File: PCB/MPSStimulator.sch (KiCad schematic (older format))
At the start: 38 parts

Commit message: WIP.
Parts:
- R? (x17): footprint Upper Center K -> (none); symbol Device:R_US -> Device:R; Notes O Bk Br Gd = 300Ω ±5% -> (none)
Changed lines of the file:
@@
 	4800 6250 4700 6250
 $Comp
-L Device:R_US R?
+L Device:R R?
 U 1 1 624C0ACD
 P 4700 6750
 F 0 "R?" H 4500 6800 50  0000 L CNN
 F 1 "180k" H 4450 6700 50  0000 L CNN
-F 2 "Upper Center K" V 4740 6740 50  0001 C CNN
+F 2 "" V 4740 6740 50  0001 C CNN
 F 3 "~" H 4700 6750 50  0001 C CNN
-F 4 "O Bk Br Gd = 300Ω ±5%" H 4700 6750 50  0001 C CNN "Notes"
+F 4 "" H 4700 6750 50  0001 C CNN "Notes"
 	1    4700 6750
 	1    0    0    1
@@
 Connection ~ 5100 7100
 $Comp
-L Device:R_US R?
+L Device:R R?
 U 1 1 625125B1
 P 5400 6550
 F 0 "R?" V 5500 6600 50  0000 L CNN
 F 1 "300" V 5500 6400 50  0000 L CNN
-F 2 "Upper Center K" V 5440 6540 50  0001 C CNN
+F 2 "" V 5440 6540 50  0001 C CNN
 F 3 "~" H 5400 6550 50  0001 C CNN
-F 4 "O Bk Br Gd = 300Ω ±5%" H 5400 6550 50  0001 C CNN "Notes"
+F 4 "" H 5400 6550 50  0001 C CNN "Notes"
 	1    5400 6550
 	0    1    1    0
@@
 	5800 6550 5550 6550
 $Comp
-L Device:R_US R?
+L Device:R R?
 U 1 1 6254B02E
 P 5400 5800
 F 0 "R?" V 5500 5850 50  0000 L CNN
 F 1 "2k4" V 5500 5700 50  0000 L CNN
-F 2 "Upper Center K" V 5440 5790 50  0001 C CNN
+F 2 "" V 5440 5790 50  0001 C CNN
 F 3 "~" H 5400 5800 50  0001 C CNN
-F 4 "O Bk Br Gd = 300Ω ±5%" H 5400 5800 50  0001 C CNN "Notes"
+F 4 "" H 5400 5800 50  0001 C CNN "Notes"
 	1    5400 5800
 	0    1    1    0
@@
 	5100 7100 6300 7100
 $Comp
-L Device:R_US R?
+L Device:R R?
 U 1 1 625BF40D
 P 5100 5250
 F 0 "R?" H 4900 5300 50  0000 L CNN
 F 1 "2k" H 4900 5200 50  0000 L CNN
-F 2 "Upper Center K" V 5140 5240 50  0001 C CNN
+F 2 "" V 5140 5240 50  0001 C CNN
 F 3 "~" H 5100 5250 50  0001 C CNN
-F 4 "O Bk Br Gd = 300Ω ±5%" H 5100 5250 50  0001 C CNN "Notes"
+F 4 "" H 5100 5250 50  0001 C CNN "Notes"
 	1    5100 5250
 	1    0    0    1
 $EndComp
 $Comp
-L Device:R_US R?
+L Device:R R?
 U 1 1 625C0721
 P 6300 5250
 F 0 "R?" H 6100 5300 50  0000 L CNN
 F 1 "1k" H 6100 5200 50  0000 L CNN
-F 2 "Upper Center K" V 6340 5240 50  0001 C CNN
+F 2 "" V 6340 5240 50  0001 C CNN
 F 3 "~" H 6300 5250 50  0001 C CNN
-F 4 "O Bk Br Gd = 300Ω ±5%" H 6300 5250 50  0001 C CNN "Notes"
+F 4 "" H 6300 5250 50  0001 C CNN "Notes"
 	1    6300 5250
 	1    0    0    1
@@
 Connection ~ 6300 7100
 $Comp
-L Device:R_US R?
+L Device:R R?
 U 1 1 6270DFA3
 P 3250 4850
 F 0 "R?" H 3050 4900 50  0000 L CNN
 F 1 "510" H 3050 4800 50  0000 L CNN
-F 2 "Upper Center K" V 3290 4840 50  0001 C CNN
+F 2 "" V 3290 4840 50  0001 C CNN
 F 3 "~" H 3250 4850 50  0001 C CNN
-F 4 "O Bk Br Gd = 300Ω ±5%" H 3250 4850 50  0001 C CNN "Notes"
+F 4 "" H 3250 4850 50  0001 C CNN "Notes"
 	1    3250 4850
 	1    0    0    1
 $EndComp
 $Comp
-L Device:R_US R?
+L Device:R R?
 U 1 1 6270E783
 P 2900 5100
 F 0 "R?" V 3000 5150 50  0000 L CNN
 F 1 "2k2" V 3000 5000 50  0000 L CNN
-F 2 "Upper Center K" V 2940 5090 50  0001 C CNN
+F 2 "" V 2940 5090 50  0001 C CNN
 F 3 "~" H 2900 5100 50  0001 C CNN
-F 4 "O Bk Br Gd = 300Ω ±5%" H 2900 5100 50  0001 C CNN "Notes"
+F 4 "" H 2900 5100 50  0001 C CNN "Notes"
 	1    2900 5100
 	0    1    1    0
@@
 	2600 5100 2750 5100
 $Comp
-L Device:R_US R?
+L Device:R R?
 U 1 1 627AC88D
 P 2150 4850
 F 0 "R?" H 1950 4900 50  0000 L CNN
 F 1 "1k2" H 1950 4800 50  0000 L CNN
-F 2 "Upper Center K" V 2190 4840 50  0001 C CNN
+F 2 "" V 2190 4840 50  0001 C CNN
 F 3 "~" H 2150 4850 50  0001 C CNN
-F 4 "O Bk Br Gd = 300Ω ±5%" H 2150 4850 50  0001 C CNN "Notes"
+F 4 "" H 2150 4850 50  0001 C CNN "Notes"
 	1    2150 4850
 	1    0    0    1
@@
 	2150 5100 2150 5000
 $Comp
-L Device:R_US R?
+L Device:R R?
 U 1 1 627EDB3A
 P 1750 5100
 F 0 "R?" V 1850 5150 50  0000 L CNN
 F 1 "240" V 1850 4950 50  0000 L CNN
-F 2 "Upper Center K" V 1790 5090 50  0001 C CNN
+F 2 "" V 1790 5090 50  0001 C CNN
 F 3 "~" H 1750 5100 50  0001 C CNN
-F 4 "O Bk Br Gd = 300Ω ±5%" H 1750 5100 50  0001 C CNN "Notes"
+F 4 "" H 1750 5100 50  0001 C CNN "Notes"
 	1    1750 5100
 	0    1    1    0
@@
 	7850 4400 8000 4400
 $Comp
-L Device:R_US R?
+L Device:R R?
 U 1 1 6213D2E2
 P 8150 4400
 F 0 "R?" H 8000 4450 50  0000 L CNN
 F 1 "20k" H 8000 4350 50  0000 L CNN
-F 2 "Upper Center K" V 8190 4390 50  0001 C CNN
+F 2 "" V 8190 4390 50  0001 C CNN
 F 3 "~" H 8150 4400 50  0001 C CNN
-F 4 "O Bk Br Gd = 300Ω ±5%" H 8150 4400 50  0001 C CNN "Notes"
+F 4 "" H 8150 4400 50  0001 C CNN "Notes"
 	1    8150 4400
 	0    -1   -1   0
@@
 	8850 4600 8850 5700
 $Comp
-L Device:R_US R?
+L Device:R R?
 U 1 1 6211D27D
 P 8850 3850
 F 0 "R?" H 8700 3900 50  0000 L CNN
 F 1 "2k" H 8700 3800 50  0000 L CNN
-F 2 "Upper Center K" V 8890 3840 50  0001 C CNN
+F 2 "" V 8890 3840 50  0001 C CNN
 F 3 "~" H 8850 3850 50  0001 C CNN
-F 4 "O Bk Br Gd = 300Ω ±5%" H 8850 3850 50  0001 C CNN "Notes"
+F 4 "" H 8850 3850 50  0001 C CNN "Notes"
 	1    8850 3850
 	-1   0    0    1
 $EndComp
 $Comp
-L Device:R_US R?
+L Device:R R?
 U 1 1 6213E6B1
 P 8450 4950
 F 0 "R?" H 8300 5000 50  0000 L CNN
 F 1 "10k" H 8300 4900 50  0000 L CNN
-F 2 "Upper Center K" V 8490 4940 50  0001 C CNN
+F 2 "" V 8490 4940 50  0001 C CNN
 F 3 "~" H 8450 4950 50  0001 C CNN
-F 4 "O Bk Br Gd = 300Ω ±5%" H 8450 4950 50  0001 C CNN "Notes"
+F 4 "" H 8450 4950 50  0001 C CNN "Notes"
 	1    8450 4950
 	1    0    0    -1
@@
 Connection ~ 8850 5700
 $Comp
-L Device:R_US R?
+L Device:R R?
 U 1 1 6214A30B
 P 9650 4350
 F 0 "R?" H 9500 4400 50  0000 L CNN
 F 1 "10k" H 9450 4300 50  0000 L CNN
-F 2 "Upper Center K" V 9690 4340 50  0001 C CNN
+F 2 "" V 9690 4340 50  0001 C CNN
 F 3 "~" H 9650 4350 50  0001 C CNN
-F 4 "O Bk Br Gd = 300Ω ±5%" H 9650 4350 50  0001 C CNN "Notes"
+F 4 "" H 9650 4350 50  0001 C CNN "Notes"
 	1    9650 4350
 	-1   0    0    1
 $EndComp
 $Comp
-L Device:R_US R?
+L Device:R R?
 U 1 1 6214AC60
 P 9650 5050
 F 0 "R?" H 9500 5100 50  0000 L CNN
 F 1 "12k" H 9450 5000 50  0000 L CNN
-F 2 "Upper Center K" V 9690 5040 50  0001 C CNN
+F 2 "" V 9690 5040 50  0001 C CNN
 F 3 "~" H 9650 5050 50  0001 C CNN
-F 4 "O Bk Br Gd = 300Ω ±5%" H 9650 5050 50  0001 C CNN "Notes"
+F 4 "" H 9650 5050 50  0001 C CNN "Notes"
 	1    9650 5050
 	-1   0    0    1
@@
 	7800 2100 7800 2250
 $Comp
-L Device:R_US R?
+L Device:R R?
 U 1 1 62182801
 P 7800 2600
 F 0 "R?" V 7700 2500 50  0000 L CNN
 F 1 "1k" V 7900 2500 50  0000 L CNN
-F 2 "Upper Center K" V 7840 2590 50  0001 C CNN
+F 2 "" V 7840 2590 50  0001 C CNN
 F 3 "~" H 7800 2600 50  0001 C CNN
-F 4 "O Bk Br Gd = 300Ω ±5%" H 7800 2600 50  0001 C CNN "Notes"
+F 4 "" H 7800 2600 50  0001 C CNN "Notes"
 	1    7800 2600
 	-1   0    0    1
@@
 $EndComp
 $Comp
-L Device:R_US R?
+L Device:R R?
 U 1 1 6207E46F
 P 5100 3200
 F 0 "R?" H 4900 3250 50  0000 L CNN
 F 1 "68k" H 4850 3150 50  0000 L CNN
-F 2 "Upper Center K" V 5140 3190 50  0001 C CNN
+F 2 "" V 5140 3190 50  0001 C CNN
 F 3 "~" H 5100 3200 50  0001 C CNN
-F 4 "O Bk Br Gd = 300Ω ±5%" H 5100 3200 50  0001 C CNN "Notes"
+F 4 "" H 5100 3200 50  0001 C CNN "Notes"
 	1    5100 3200
 	1    0    0    1
@@
 	5600 2200 5100 2200
 $Comp
-L Device:R_US R?
+L Device:R R?
 U 1 1 620C6553
 P 5450 3200
 F 0 "R?" H 5250 3250 50  0000 L CNN
 F 1 "68k" H 5200 3150 50  0000 L CNN
-F 2 "Upper Center K" V 5490 3190 50  0001 C CNN
+F 2 "" V 5490 3190 50  0001 C CNN
 F 3 "~" H 5450 3200 50  0001 C CNN
-F 4 "O Bk Br Gd = 300Ω ±5%" H 5450 3200 50  0001 C CNN "Notes"
+F 4 "" H 5450 3200 50  0001 C CNN "Notes"
 	1    5450 3200
 	1    0    0    1

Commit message: Completed schematic. Started work on PCB.
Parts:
- added TP1: AT1, TestPoint:TestPoint_Pad_3.0x3.0mm, symbol Connector:TestPoint
- added TP2: AT2, TestPoint:TestPoint_Pad_3.0x3.0mm, symbol Connector:TestPoint
- added TP3: 5195TR, Britishideas:5190TR-Colored-Test-Point, symbol Connector:TestPoint
- added TP4, TP5, TP6, TP7: 5194TR, Britishideas:5190TR-Colored-Test-Point, symbol Connector:TestPoint
- added TP8: BIAS1, TestPoint:TestPoint_Pad_3.0x3.0mm, symbol Connector:TestPoint
- added TP9: BIAS2, TestPoint:TestPoint_Pad_3.0x3.0mm, symbol Connector:TestPoint
- C17, C18, C19: renamed from C?; footprint Right D Line -> Capacitor_SMD:C_0603_1608Metric
- D4, D5, D6, D7, D8: renamed from D?; value DIODE -> RB520SM-30T2R; footprint (none) -> Diode_SMD:D_SOD-523; manf# (none) -> RB520SM-30T2R
- Q1, Q2, Q3, Q4, Q5: renamed from Q?; value BCY58 -> PZT2222A,115; footprint Package_TO_SOT_THT:TO-92_Inline -> Package_TO_SOT_SMD:SOT-223-3_TabPin2; symbol Transistor_BJT:BC547 -> Transistor_BJT:2SD1047; Notes Center K -> (none); manf# (none) -> PZT2222A,115
- R10, R11, R12, R13, R14, R15, R16, R17, R18, R19, R20, R21, R22, R23, R24, R25, R26, R27, R28, R29, R30, R31, R32: renamed from R?; footprint (none) -> Resistor_SMD:R_0603_1608Metric
- RV1: renamed from RV?; footprint (none) -> Britishideas:Surface_Mount_Cermet_Trimmer_SM-42-43W; symbol Device:Varistor -> Device:R_Variable; manf# (none) -> SM-43TW102
- RV2: renamed from RV?; footprint (none) -> Britishideas:Surface_Mount_Cermet_Trimmer_SM-42-43W; symbol Device:Varistor -> Device:R_Variable; manf# (none) -> SM-43TW502
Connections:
- wire segments 120 -> 136
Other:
- note added: "BROWN"
- note added: "YELLOW"
- moved on the sheet: R27

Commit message: Working on PCB layout.
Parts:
- TP1, TP2, TP8, TP9: footprint TestPoint:TestPoint_Pad_3.0x3.0mm -> TestPoint:TestPoint_Pad_2.0x2.0mm
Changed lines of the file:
@@
 F 0 "TP2" V 1045 6022 50  0000 C CNN
 F 1 "AT2" V 954 6022 50  0000 C CNN
-F 2 "TestPoint:TestPoint_Pad_3.0x3.0mm" H 1050 5950 50  0001 C CNN
+F 2 "TestPoint:TestPoint_Pad_2.0x2.0mm" H 1050 5950 50  0001 C CNN
 F 3 "~" H 1050 5950 50  0001 C CNN
 	1    850  5950
@@
 F 0 "TP1" V 1045 5172 50  0000 C CNN
 F 1 "AT1" V 954 5172 50  0000 C CNN
-F 2 "TestPoint:TestPoint_Pad_3.0x3.0mm" H 1050 5100 50  0001 C CNN
+F 2 "TestPoint:TestPoint_Pad_2.0x2.0mm" H 1050 5100 50  0001 C CNN
 F 3 "~" H 1050 5100 50  0001 C CNN
 	1    850  5100
@@
 F 0 "TP8" V 8245 1672 50  0000 C CNN
 F 1 "BIAS1" V 8154 1672 50  0000 C CNN
-F 2 "TestPoint:TestPoint_Pad_3.0x3.0mm" H 8250 1600 50  0001 C CNN
+F 2 "TestPoint:TestPoint_Pad_2.0x2.0mm" H 8250 1600 50  0001 C CNN
 F 3 "~" H 8250 1600 50  0001 C CNN
 	1    8050 1600
@@
 F 0 "TP9" V 8245 2172 50  0000 C CNN
 F 1 "BIAS2" V 8154 2172 50  0000 C CNN
-F 2 "TestPoint:TestPoint_Pad_3.0x3.0mm" H 8250 2100 50  0001 C CNN
+F 2 "TestPoint:TestPoint_Pad_2.0x2.0mm" H 8250 2100 50  0001 C CNN
 F 3 "~" H 8250 2100 50  0001 C CNN
 	1    8050 2100

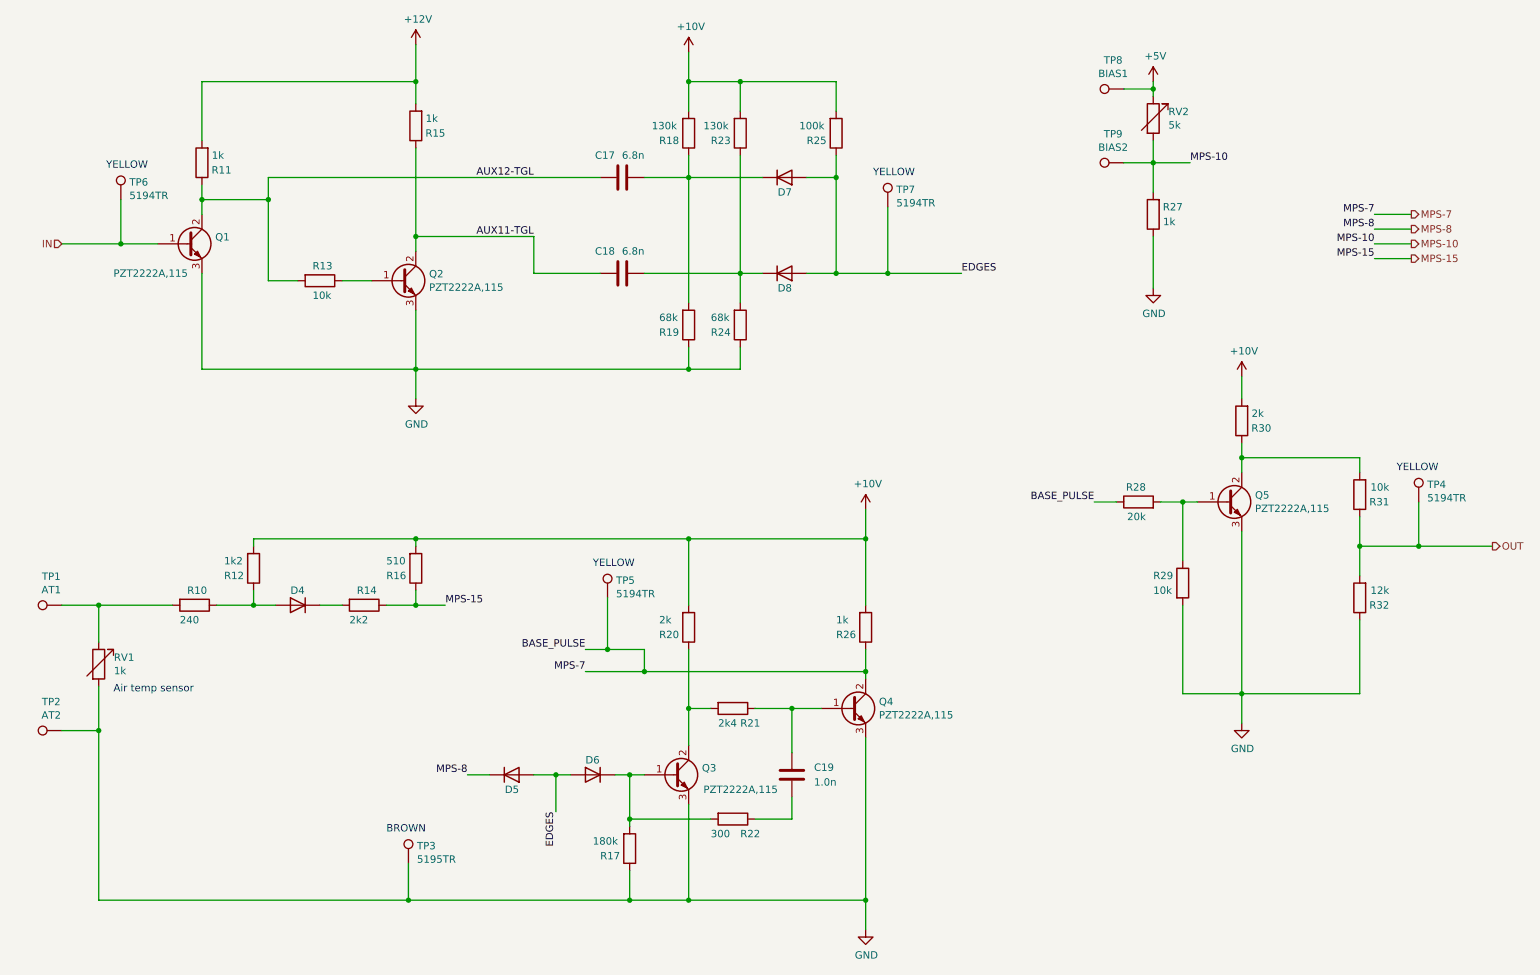
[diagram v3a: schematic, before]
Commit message: Added status LED, remove LCD connectors, changed MPS connector to screw terminal block, added 12V power connections, removed 5V to 12V boost converter. Completely reworked PCB. Removed old PCB CAD files.
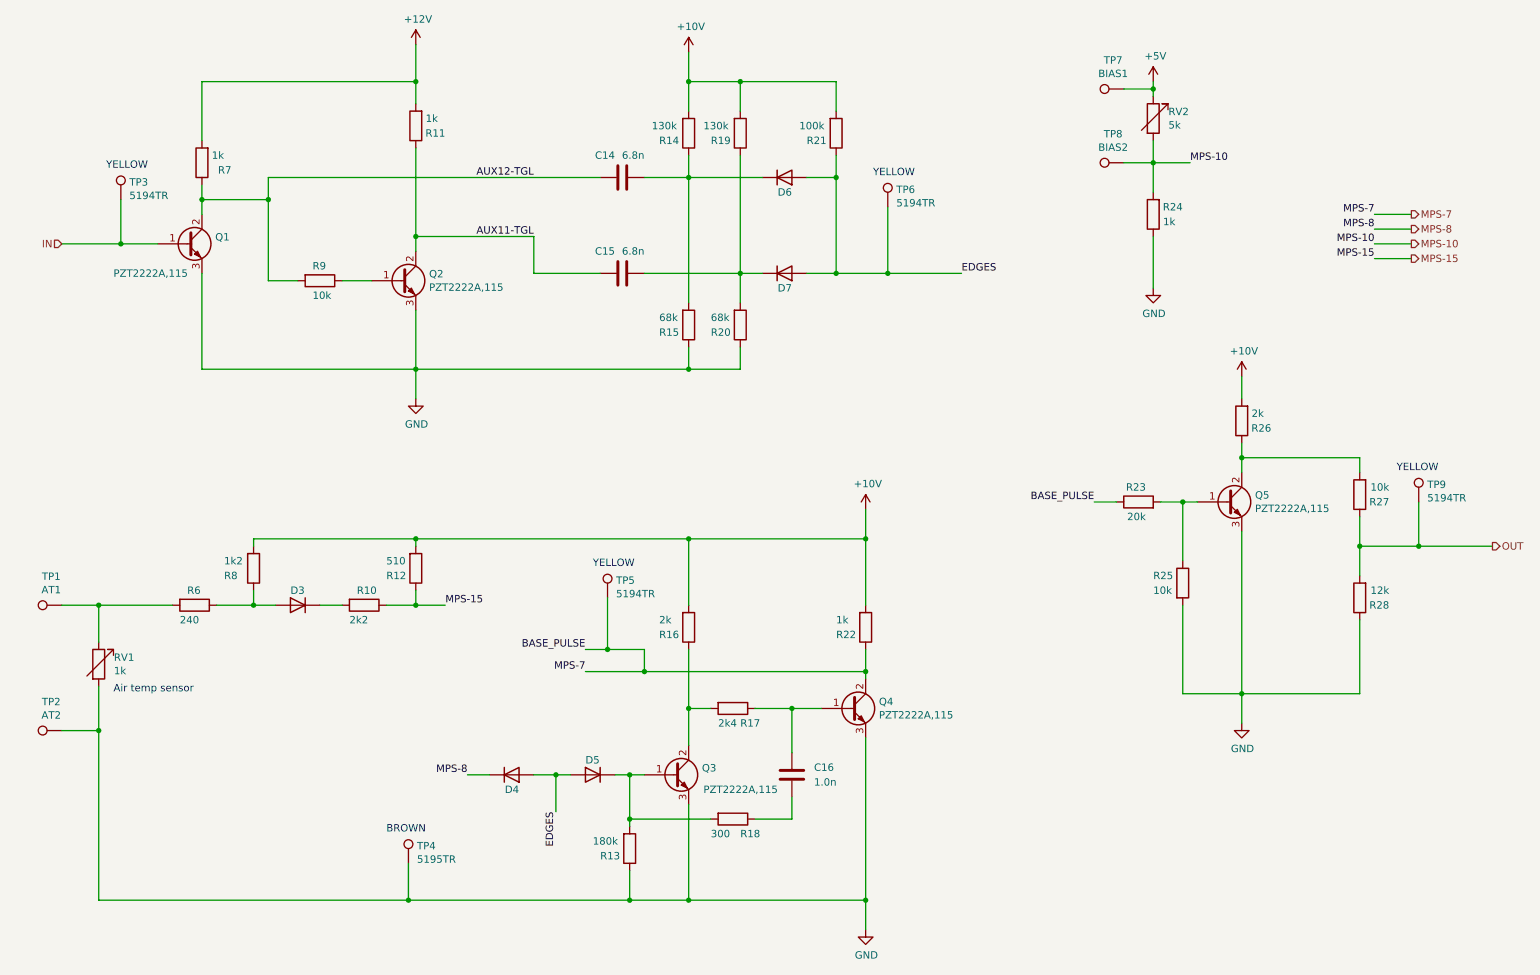
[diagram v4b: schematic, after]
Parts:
- renumbered C17 to C14, C18 to C15, C19 to C16, D4 to D3, D5 to D4, D6 to D5, D7 to D6, D8 to D7, R14 to R10, R15 to R11, R16 to R12, R17 to R13, R18 to R14, R19 to R15, R20 to R16, R21 to R17, R22 to R18, R23 to R19, R24 to R20, R25 to R21, R26 to R22, R28 to R23, R27 to R24, R29 to R25, R30 to R26, R31 to R27, R32 to R28, R10 to R6, R11 to R7, R12 to R8, R13 to R9, TP6 to TP3, TP3 to TP4, TP7 to TP6, TP8 to TP7, TP9 to TP8, TP4 to TP9

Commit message: Added LED for 12V power. Added resistor on MPS_STIMULUS signal. Moved track away from mounting hole. Fixed orientation of diodes. Added PDF of schematic. Updated manufacturing files.
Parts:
- added R30: 10k, Resistor_SMD:R_0603_1608Metric, symbol Device:R
- D3, D4, D5, D6, D7: symbol Simulation_SPICE:DIODE -> Device:D
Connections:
- net EDGES: now also D4.2 (A), D5.2 (A), D6.2 (A), D7.2 (A); no longer D4.1 (A), D5.1 (A), D6.1 (A), D7.1 (A)
- net IN: now also R30.2; no longer Q1.1 (B), TP3.1
- net MPS-8: now also D4.1 (K); no longer D4.2 (K)
- net at C14.2, R14.1, R15.2: now also D6.1 (K); no longer D6.2 (K)
- net at C15.2, R19.1, R20.2: now also D7.1 (K); no longer D7.2 (K)
- net at Q3.1 (B), R13.2, R18.2: now also D5.1 (K); no longer D5.2 (K)
- net at R10.2: now also D3.1 (K); no longer D3.2 (K)
- net at R6.1, R8.1: now also D3.2 (A); no longer D3.1 (A)
- new net: Q1.1 (B), R30.1, TP3.1
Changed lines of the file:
@@
 Sheet 3 3
 Title "MPS Tune-o-Matic"
-Date "2022-10-31"
-Rev "V1.0"
+Date "2022-11-10"
+Rev "V1.1"
 Comp "(C) andy@britishideas.com 2022"
 Comment1 "For Bosch D-Jetronic MPS Type 3"
@@
 $EndDescr
 $Comp
-L Simulation_SPICE:DIODE D4
+L Device:D D4
 U 1 1 62457901
 P 3900 6250
@@
 F 6 "RB520SM-30T2R" H 3900 6250 50  0001 C CNN "manf#"
 	1    3900 6250
-	-1   0    0    -1
-$EndComp
-$Comp
-L Simulation_SPICE:DIODE D5
+	1    0    0    1
+$EndComp
+$Comp
+L Device:D D5
 U 1 1 62458057
 P 4450 6250
-F 0 "D5" H 4400 6150 50  0000 L CNN
+F 0 "D5" H 4400 6350 50  0000 L CNN
 F 1 "RB520SM-30T2R" V 4495 6330 50  0001 L CNN
 F 2 "Diode_SMD:D_SOD-523" H 4450 6250 50  0001 C CNN
@@
 F 6 "RB520SM-30T2R" H 4450 6250 50  0001 C CNN "manf#"
 	1    4450 6250
-	1    0    0    1
+	-1   0    0    -1
 $EndComp
 Wire Wire Line
@@
 	3250 5100 3050 5100
 $Comp
-L Simulation_SPICE:DIODE D3
+L Device:D D3
 U 1 1 6278C325
 P 2450 5100
@@
 F 6 "RB520SM-30T2R" H 2450 5100 50  0001 C CNN "manf#"
 	1    2450 5100
-	1    0    0    1
+	-1   0    0    -1
 $EndComp
 Wire Wire Line
@@
 $EndComp
 Wire Wire Line
-	850  2650 1250 2650
+	1150 2650 1250 2650
 Wire Wire Line
 	1800 2450 1800 2350
@@
 Connection ~ 5100 2200
 $Comp
-L Simulation_SPICE:DIODE D6
+L Device:D D6
 U 1 1 620A24B9
 P 5750 2200
@@
 F 6 "RB520SM-30T2R" H 5750 2200 50  0001 C CNN "manf#"
 	1    5750 2200
-	-1   0    0    -1
+	1    0    0    1
 $EndComp
 Wire Wire Line
@@
 	5450 2850 5450 3050
 $Comp
-L Simulation_SPICE:DIODE D7
+L Device:D D7
 U 1 1 620FD22E
 P 5750 2850
@@
 F 6 "RB520SM-30T2R" H 5750 2850 50  0001 C CNN "manf#"
 	1    5750 2850
-	-1   0    0    -1
+	1    0    0    1
 $EndComp
 Wire Wire Line
@@
 	0    -1   1    0
 $EndComp
-Text HLabel 850  2650 0    50   Input ~ 0
+Text HLabel 700  2650 0    50   Input ~ 0
 IN
 Wire Wire Line
@@
 Wire Wire Line
 	8250 1600 8250 1550
+$Comp
+L Device:R R30
+U 1 1 636DCAD5
+P 1000 2650
+F 0 "R30" V 900 2600 50  0000 L CNN
+F 1 "10k" V 1100 2600 50  0000 L CNN
+F 2 "Resistor_SMD:R_0603_1608Metric" V 1040 2640 50  0001 C CNN
+F 3 "~" H 1000 2650 50  0001 C CNN
+F 4 "" H 1000 2650 50  0001 C CNN "Notes"
+	1    1000 2650
+	0    1    1    0
+$EndComp
+Wire Wire Line
+	700  2650 850  2650
 $EndSCHEMATC
